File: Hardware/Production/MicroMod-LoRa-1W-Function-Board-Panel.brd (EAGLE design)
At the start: 96.6 x 150.8 mm, 202 parts, among them J1 MICROMOD_STANDARD, J11 MICROMOD_STANDARD, J2 MICROMOD_STANDARD, J3 MICROMOD_STANDARD, Q1 20V/4.2A/52mΩ/1.4W, Q10 600mA/40V, Q11 20V/4.2A/52mΩ/1.4W, Q12 600mA/40V, Q13 20V/4.2A/52mΩ/1.4W, Q14 600mA/40V, Q15 20V/4.2A/52mΩ/1.4W, Q16 600mA/40V, Q2 600mA/40V, Q3 20V/4.2A/52mΩ/1.4W, Q4 600mA/40V, Q5 20V/4.2A/52mΩ/1.4W, Q6 600mA/40V, Q7 20V/4.2A/52mΩ/1.4W, Q8 600mA/40V, Q9 20V/4.2A/52mΩ/1.4W, U1 EEPROM, U2 E19-915M30S, U3 EEPROM, U4 E19-915M30S, U5 E19-915M30S, U6 EEPROM, U7 E19-915M30S, U8 EEPROM

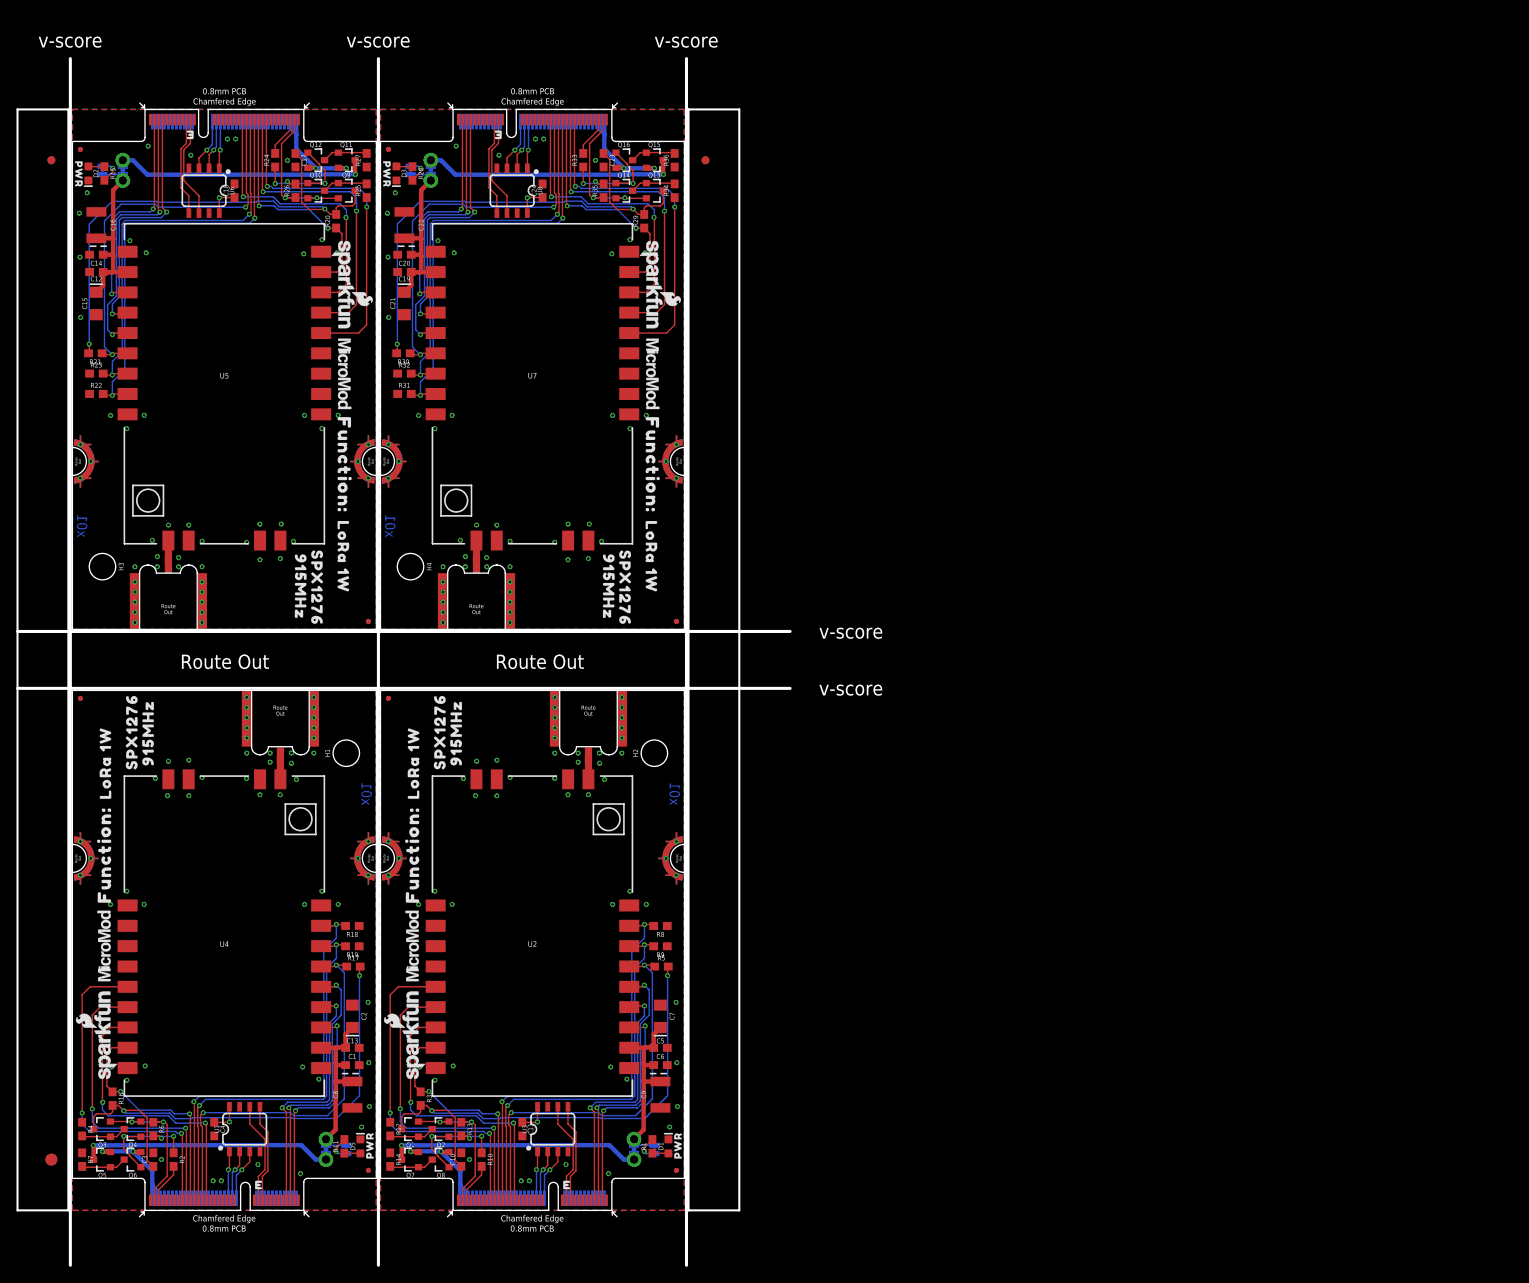
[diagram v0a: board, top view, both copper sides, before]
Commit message: Fix power control circuit. Add example sketch. Add x02 production panels.
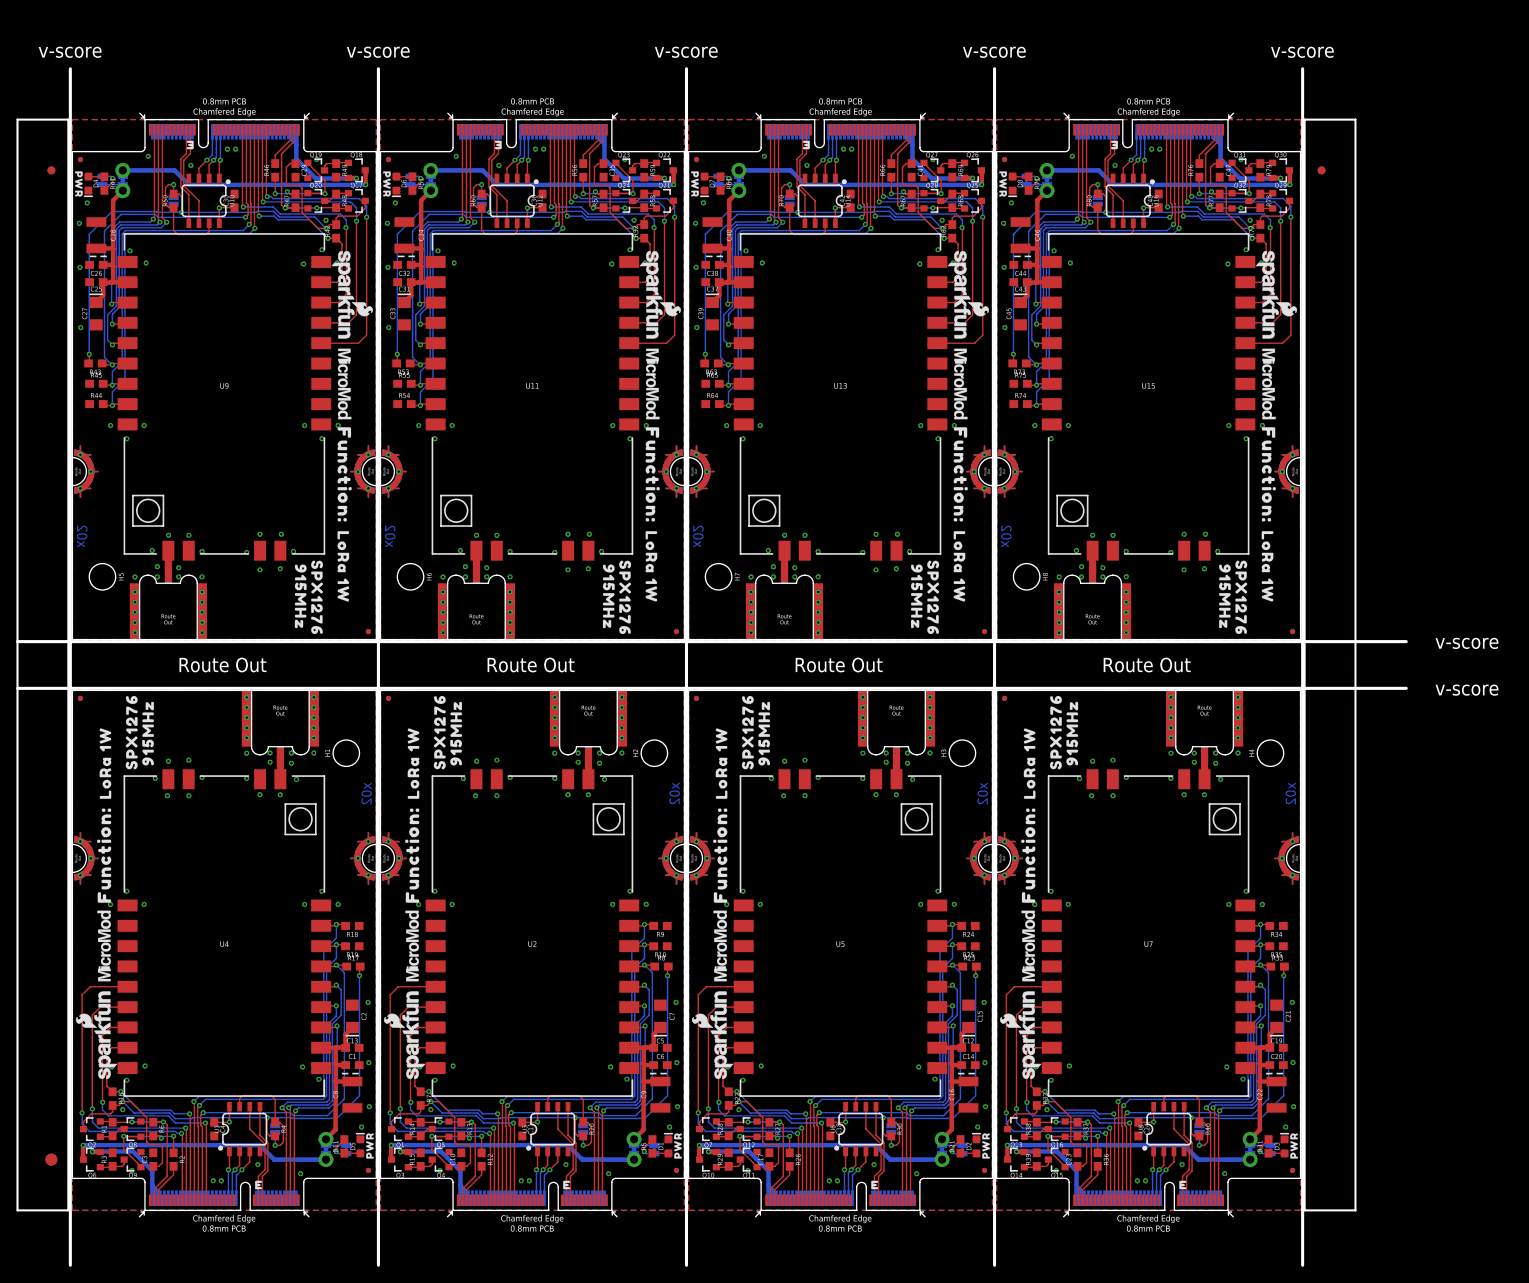
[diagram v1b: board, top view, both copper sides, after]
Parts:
- added C25, C31, C37, C43: 0.22uF, SparkFun-Capacitors:0603
- added C26, C29, C30, C32, C35, C36, C38, C41, C42, C44, C47, C48: 0.1uF, SparkFun-Capacitors:0603
- added C27, C33, C39, C45: 10uF, SparkFun-Capacitors:EIA3216
- added C28, C34, C40, C46: 47uF, SparkFun-Capacitors:EIA3528
- added D4, D6, D7, D8: RED, SparkFun-LED:LED-0603
- added E5, E6, E7, E8: RP-SMA, SparkFun-RF:SMA-EDGE-SMD
- added FD17, FD18, FD19, FD20, FD21, FD22, FD23, FD24, FD25, FD26, FD27, FD28, FD29, FD30, FD31, FD32: FIDUCIALUFIDUCIAL, SparkFun-Aesthetics:FIDUCIAL-MICRO
- added H5, H6, H7, H8: STAND-OFF, SparkFun-Hardware:STAND-OFF
- added J4, J5, J6, J7: MICROMOD_STANDARD, SparkFun-MicroMod-Function:M.2-CARD-E-22_FUNCTION_STANDARD
- added JP1, JP2, JP3, JP4, JP5, JP6, JP7, JP8: (no value), SparkFun-Jumpers:SMT-JUMPER_2_NO_SILK
- added LOGO13, LOGO15, LOGO16, LOGO18, LOGO19, LOGO21, LOGO22, LOGO24: SFE_LOGO_NAME_FLAME.1_INCH, SparkFun-Aesthetics:SFE_LOGO_NAME_FLAME_.1
- added LOGO14, LOGO17, LOGO20, LOGO23: OSHW-LOGOMINI, SparkFun-Aesthetics:OSHW-LOGO-MINI
- added MEAS4, MEAS5, MEAS6, MEAS7: (no value), SparkFun-Jumpers:COMBO-JUMPER_2_NC_TRACE
- added PWR_LED4, PWR_LED5, PWR_LED6, PWR_LED7: (no value), SparkFun-Jumpers:SMT-JUMPER_2_NC_TRACE_SILK
- added Q17, Q18, Q21, Q22, Q25, Q26, Q29, Q30: 20V/4.2A/52mΩ/1.4W, SparkFun-DiscreteSemi:SOT23-3
- added Q19, Q20, Q23, Q24, Q27, Q28, Q31, Q32: 5.8A/30V/35mΩ, SparkFun-DiscreteSemi:SOT23-3
- added R37, R42, R43, R44, R45, R47, R52, R53, R54, R55, R57, R62, R63, R64, R65, R67, R72, R73, R74, R75, R77: 100k, SparkFun-Resistors:0603
- added R38, R39, R40, R48, R49, R50, R58, R59, R60, R68, R69, R70, R78, R79, R80: 10k, SparkFun-Resistors:0603
- added R41, R51, R61, R71: 1k, SparkFun-Resistors:0603
- added R46, R56, R66, R76: 470, SparkFun-Resistors:0603
- added U$100, U$108, U$116, U$124, U$68, U$76, U$84, U$92: (no value), output:1W1
- added U$101, U$107, U$117, U$123, U$69, U$75, U$85, U$91: (no value), output:915MHZ2
- added U$102, U$105, U$118, U$121, U$70, U$73, U$86, U$89: (no value), output:LORA0
- added U$103, U$106, U$119, U$122, U$71, U$74, U$87, U$90: (no value), output:SPX12763
- added U$104, U$120, U$72, U$88: (no value), output:PWR0
- added U$109, U$111, U$125, U$127, U$60, U$62, U$77, U$79, U$93, U$95: (no value), output:FUNCTION#0
- added U$110, U$126, U$61, U$78, U$94: (no value), output:#PWR#0
- added U$112, U$128, U$64, U$80, U$96: (no value), output:#WP#0
- added U$113, U$114, U$65, U$66, U$81, U$82, U$97, U$98: (no value), SparkFun-MicroMod:MICROMOD_LOGO_.35
- added U$115, U$67, U$83, U$99: (no value), output:#MEAS#3
- added U10, U12, U14, U16: EEPROM, SparkFun-IC-Memory:SO08
- added U11, U13, U15, U9: E19-915M30S, SparkFun-RF:E19-915MS1W
- C16, C22, C8, C9: value 68uF -> 47uF
- Q10, Q14, Q2, Q6: value 600mA/40V -> 20V/4.2A/52mΩ/1.4W
- Q11, Q15, Q5, Q9: value 20V/4.2A/52mΩ/1.4W -> 5.8A/30V/35mΩ
- Q12, Q16, Q4, Q8: value 600mA/40V -> 5.8A/30V/35mΩ
- R1, R15, R28: value 1k -> 10k
- R10, R24, R33: value 470 -> 100k
- R12, R26, R36: value 100k -> 470
- R14, R20, R29, R3, R30, R4: value 100k -> 10k
- R21, R31, R5: value 100k -> 1k
- U$10, U$26: device SparkFun-MicroMod:MICROMOD_LOGO_.35 -> output:#WP#0
- U$12, U$31: device output:#MEAS#3 -> SparkFun-MicroMod:MICROMOD_LOGO_.35
- U$13: device output:1W1 -> output:#MEAS#3
- U$14: device output:915MHZ2 -> output:1W1
- U$15: device output:LORA0 -> output:915MHZ2
- U$16, U$19: device output:SPX12763 -> output:LORA0
- U$17: device output:PWR0 -> output:SPX12763
- U$18: device output:LORA0 -> output:PWR0
- U$20: device output:915MHZ2 -> output:SPX12763
- U$21: device output:1W1 -> output:915MHZ2
- U$22, U$59: device output:FUNCTION#0 -> output:1W1
- U$23: device output:#PWR#0 -> output:FUNCTION#0
- U$24: device output:FUNCTION#0 -> output:#PWR#0
- U$25, U$46: device SparkFun-MicroMod:MICROMOD_LOGO_.35 -> output:FUNCTION#0
- U$32, U$48: device output:1W1 -> SparkFun-MicroMod:MICROMOD_LOGO_.35
- U$33: device output:915MHZ2 -> output:#MEAS#3
- U$34: device output:LORA0 -> output:1W1
- U$35: device output:SPX12763 -> output:915MHZ2
- U$36: device output:PWR0 -> output:LORA0
- U$38: device output:LORA0 -> output:SPX12763
- U$39: device output:SPX12763 -> output:PWR0
- U$40: device output:915MHZ2 -> output:LORA0
- U$41: device output:1W1 -> output:SPX12763
- U$42: device output:FUNCTION#0 -> output:915MHZ2
- U$43: device output:#PWR#0 -> output:1W1
- U$45: device SparkFun-MicroMod:MICROMOD_LOGO_.35 -> output:#PWR#0
- U$47: device output:#MEAS#3 -> output:#WP#0
- U$49: device output:915MHZ2 -> SparkFun-MicroMod:MICROMOD_LOGO_.35
- U$50: device output:LORA0 -> output:#MEAS#3
- U$51: device output:SPX12763 -> output:1W1
- U$52: device output:PWR0 -> output:915MHZ2
- U$55: device output:915MHZ2 -> output:PWR0
- U$56: device output:1W1 -> output:LORA0
- U$57: device output:FUNCTION#0 -> output:SPX12763
- U$58: device output:#PWR#0 -> output:915MHZ2
- moved FD13 170.5 mm to (152.5, 5.00), turned to 90 degrees
- moved FD15 170.5 mm to (152.5, 5.00), turned to 270 degrees
- moved FD11 170.5 mm to (114.0, 5.00), turned to 270 degrees
- moved FD9 170.5 mm to (114.0, 5.00), turned to 90 degrees
- moved D3 164.7 mm to (151.5, 8.00), turned to 90 degrees
- moved D2 164.7 mm to (113.0, 8.00), turned to 90 degrees
- moved PWR_LED3 162.9 mm to (149.8, 7.62), turned to 90 degrees
- moved PWR_LED2 162.9 mm to (111.3, 7.62), turned to 90 degrees
- moved MEAS3 159.6 mm to (147.2, 7.62), turned to 90 degrees
- moved MEAS2 159.6 mm to (108.7, 7.62), turned to 90 degrees
- moved J3 157.7 mm to (134.5, 0.00), turned to 0 degrees
- moved J2 157.7 mm to (96.0, 0.00), turned to 0 degrees
- moved C22 153.9 mm to (150.5, 14.5), turned to 90 degrees
- moved C16 153.9 mm to (112.0, 14.5), turned to 90 degrees
- moved C20 148.8 mm to (150.5, 18.2), turned to 0 degrees
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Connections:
- removed net N$10 (its old number): Q1.1, Q2.3, R12.2
- removed net N$17 (its old number): Q10.3, Q9.1, R25.2
- removed net N$24 (its old number): Q15.1, Q16.3, R36.2
- new net 3.3V4: C29.1, C30.1, Q17.3, R42.2, R43.2, R50.2, U10.8
- new net 3.3V5: C35.1, C36.1, Q21.3, R52.2, R53.2, R60.2, U12.8
- new net 3.3V6: C41.1, C42.1, Q25.3, R62.2, R63.2, R70.2, U14.8
- new net 3.3V7: C47.1, C48.1, Q29.3, R72.2, R73.2, R80.2, U16.8
- new net 3.3V_IN4: J4.73, Q17.2, R47.1, R48.2
- new net 3.3V_IN5: J5.73, Q21.2, R57.1, R58.2
- new net 3.3V_IN6: J6.73, Q25.2, R67.1, R68.2
- new net 3.3V_IN7: J7.73, Q29.2, R77.1, R78.2
- new net 5V4: C25.1, C26.1, C27.+, C28.A, MEAS4.2, MEAS4.4, PWR_LED4.2, U9.11
- new net 5V5: C31.1, C32.1, C33.+, C34.A, MEAS5.2, MEAS5.4, PWR_LED5.2, U11.11
- new net 5V6: C37.1, C38.1, C39.+, C40.A, MEAS6.2, MEAS6.4, PWR_LED6.2, U13.11
- new net 5V7: C43.1, C44.1, C45.+, C46.A, MEAS7.2, MEAS7.4, PWR_LED7.2, U15.11
- new net A12: J4.36, U10.1
- new net A13: J4.32, U10.3
- new net A14: J4.34, U10.2
- new net A15: J5.36, U12.1
- new net A16: J5.32, U12.3
- new net A17: J5.34, U12.2
- new net A18: J6.36, U14.1
- new net A19: J6.32, U14.3
- new net A20: J6.34, U14.2
- new net A21: J7.36, U16.1
- new net A22: J7.32, U16.3
- new net A23: J7.34, U16.2
- new net GND4: C25.2, C26.2, C27.-, C28.C, C29.2, C30.2, D4.C, E5.GND@0, E5.GND@1, J4.1, J4.33, J4.39, J4.45, J4.75, J4.GND1, J4.GND2, J4.GND3, J4.GND4, J4.GND5, J4.GND6, JP5.1, Q19.2, Q20.2, R44.1, R45.1, U10.4, U9.1, U9.10, U9.18, U9.20, U9.21, U9.22, U9.9
- new net GND5: C31.2, C32.2, C33.-, C34.C, C35.2, C36.2, D6.C, E6.GND@0, E6.GND@1, J5.1, J5.33, J5.39, J5.45, J5.75, J5.GND1, J5.GND2, J5.GND3, J5.GND4, J5.GND5, J5.GND6, JP6.1, Q23.2, Q24.2, R54.1, R55.1, U11.1, U11.10, U11.18, U11.20, U11.21, U11.22, U11.9, U12.4
- new net GND6: C37.2, C38.2, C39.-, C40.C, C41.2, C42.2, D7.C, E7.GND@0, E7.GND@1, J6.1, J6.33, J6.39, J6.45, J6.75, J6.GND1, J6.GND2, J6.GND3, J6.GND4, J6.GND5, J6.GND6, JP7.1, Q27.2, Q28.2, R64.1, R65.1, U13.1, U13.10, U13.18, U13.20, U13.21, U13.22, U13.9, U14.4
- new net GND7: C43.2, C44.2, C45.-, C46.C, C47.2, C48.2, D8.C, E8.GND@0, E8.GND@1, J7.1, J7.33, J7.39, J7.45, J7.75, J7.GND1, J7.GND2, J7.GND3, J7.GND4, J7.GND5, J7.GND6, JP8.1, Q31.2, Q32.2, R74.1, R75.1, U15.1, U15.10, U15.18, U15.20, U15.21, U15.22, U15.9, U16.4
- new net I2C_SCL4: J4.21, U10.6
- new net I2C_SCL5: J5.21, U12.6
- new net I2C_SCL6: J6.21, U14.6
- new net I2C_SCL7: J7.21, U16.6
- new net I2C_SDA4: J4.19, U10.5
- new net I2C_SDA5: J5.19, U12.5
- new net I2C_SDA6: J6.19, U14.5
- new net I2C_SDA7: J7.19, U16.5
- new net LORA_!CS!4: J4.49, R43.1, U9.15
- new net LORA_!CS!5: J5.49, R53.1, U11.15
- new net LORA_!CS!6: J6.49, R63.1, U13.15
- new net LORA_!CS!7: J7.49, R73.1, U15.15
- new net LORA_!RST!4: J4.55, R42.1, U9.8
- new net LORA_!RST!5: J5.55, R52.1, U11.8
- new net LORA_!RST!6: J6.55, R62.1, U13.8
- new net LORA_!RST!7: J7.55, R72.1, U15.8
- new net LORA_D12: J4.47, U9.7
- new net LORA_D13: J4.57, U9.6
- new net LORA_D14: J4.59, U9.5
- new net LORA_D15: J5.47, U11.7
- new net LORA_D16: J5.57, U11.6
- new net LORA_D17: J5.59, U11.5
- new net LORA_D18: J6.47, U13.7
- new net LORA_D19: J6.57, U13.6
- new net LORA_D20: J6.59, U13.5
- new net LORA_D21: J7.47, U15.7
- new net LORA_D22: J7.57, U15.6
- new net LORA_D23: J7.59, U15.5
- new net LORA_RXEN4: J4.53, R44.2, U9.17
- new net LORA_RXEN5: J5.53, R54.2, U11.17
- new net LORA_RXEN6: J6.53, R64.2, U13.17
- new net LORA_RXEN7: J7.53, R74.2, U15.17
- new net LORA_TXEN4: J4.51, R45.2, U9.16
- new net LORA_TXEN5: J5.51, R55.2, U11.16
- new net LORA_TXEN6: J6.51, R65.2, U13.16
- new net LORA_TXEN7: J7.51, R75.2, U15.16
- new net N$15: PWR_LED2.1, R21.2
- new net N$21: JP3.2, R30.1, U6.7
- new net N$25: J3.71, R36.2
- new net N$26: Q13.1, Q16.3, R38.1
- new net N$27: Q14.1, Q15.3, R39.1
- new net N$28: JP4.2, R40.1, U8.7
- new net N$29: PWR_LED4.1, R41.2
- new net N$30: D4.A, R41.1
- new net N$31: E5.SIG, U9.19
- new net N$32: J4.71, R46.2
- new net N$33: Q17.1, Q20.3, R48.1
- new net N$34: Q18.1, Q19.3, R49.1
- new net N$35: JP5.2, R50.1, U10.7
- new net N$36: PWR_LED5.1, R51.2
- new net N$37: D6.A, R51.1
- new net N$38: E6.SIG, U11.19
- new net N$39: J5.71, R56.2
- new net N$40: Q21.1, Q24.3, R58.1
- new net N$41: Q22.1, Q23.3, R59.1
- new net N$42: JP6.2, R60.1, U12.7
- new net N$43: PWR_LED6.1, R61.2
- new net N$44: D7.A, R61.1
- new net N$45: E7.SIG, U13.19
- new net N$46: J6.71, R66.2
- new net N$47: Q25.1, Q28.3, R68.1
- new net N$48: Q26.1, Q27.3, R69.1
- new net N$49: JP7.2, R70.1, U14.7
- new net N$50: PWR_LED7.1, R71.2
- new net N$51: D8.A, R71.1
- new net N$52: E8.SIG, U15.19
- new net N$53: J7.71, R76.2
- new net N$54: Q29.1, Q32.3, R78.1
- new net N$55: Q30.1, Q31.3, R79.1
- new net N$56: JP8.2, R80.1, U16.7
- new net N$7: JP1.2, R4.1, U1.7
- new net PWR_EN4: Q19.1, Q20.1, R46.1, R47.2
- new net PWR_EN5: Q23.1, Q24.1, R56.1, R57.2
- new net PWR_EN6: Q27.1, Q28.1, R66.1, R67.2
- new net PWR_EN7: Q31.1, Q32.1, R76.1, R77.2
- new net SPI_CIPO4: J4.7, U9.13
- new net SPI_CIPO5: J5.7, U11.13
- new net SPI_CIPO6: J6.7, U13.13
- new net SPI_CIPO7: J7.7, U15.13
- new net SPI_COPI4: J4.5, U9.14
- new net SPI_COPI5: J5.5, U11.14
- new net SPI_COPI6: J6.5, U13.14
- new net SPI_COPI7: J7.5, U15.14
- new net SPI_SCK4: J4.3, U9.12
- new net SPI_SCK5: J5.3, U11.12
- new net SPI_SCK6: J6.3, U13.12
- new net SPI_SCK7: J7.3, U15.12
- new net VCC4: MEAS4.1, MEAS4.3, Q18.3
- new net VCC5: MEAS5.1, MEAS5.3, Q22.3
- new net VCC6: MEAS6.1, MEAS6.3, Q26.3
- new net VCC7: MEAS7.1, MEAS7.3, Q30.3
- new net VCC_IN4: J4.72, J4.74, Q18.2, R49.2
- new net VCC_IN5: J5.72, J5.74, Q22.2, R59.2
- new net VCC_IN6: J6.72, J6.74, Q26.2, R69.2
- new net VCC_IN7: J7.72, J7.74, Q30.2, R79.2
- net 3.3V: now also Q2.3, R4.2; no longer Q3.3
- net 3.3V1: now also R20.2, R7.2, R8.2; no longer R3.2, R5.2
- net 3.3V2: now also Q7.3, R22.2, R23.2, R30.2; no longer Q9.3, R20.2, R21.2
- net 3.3V3: now also R32.2, R33.2, R40.2; no longer R29.2, R30.2
- net 3.3V_IN: now also Q2.2, R1.2; no longer Q3.2, Q4.2
- net 3.3V_IN1: now also R14.2; no longer Q2.2
- net 3.3V_IN2: now also Q7.2, R27.1, R28.2; no longer Q10.2, Q9.2, R26.1
- net 3.3V_IN3: now also R37.1, R38.2; no longer Q14.2, R35.1
- net GND: now also JP1.1, Q8.2, Q9.2; no longer R4.1, R7.1, U1.7
- net GND1: now also JP2.1, Q4.2, Q5.2, R10.1; no longer R12.1, R14.1, R8.1, U3.7
- net GND2: now also JP3.1, Q11.2, Q12.2, R24.1; no longer R22.1, R23.1, R27.1, U6.7
- net GND3: now also JP4.1, Q15.2, Q16.2, R35.1; no longer R31.1, R32.1, R36.1, U8.7
- net LORA_!CS!1: now also R8.1; no longer R5.1
- net LORA_!CS!2: now also R23.1; no longer R21.1
- net LORA_!CS!3: now also R33.1; no longer R30.1
- net LORA_!RST!1: now also R7.1; no longer R3.1
- net LORA_!RST!2: now also R22.1; no longer R20.1
- net LORA_!RST!3: now also R32.1; no longer R29.1
- net LORA_RXEN1: now also R9.2; no longer R8.2
- net LORA_RXEN2: now also R24.2; no longer R22.2
- net LORA_RXEN3: now also R34.2; no longer R31.2
- net LORA_TXEN1: now also R10.2; no longer R9.2
- net LORA_TXEN2: now also R25.2; no longer R23.2
- net LORA_TXEN3: now also R35.2; no longer R32.2
- net N$11: now also J1.71, R12.2; no longer Q5.1, Q6.3, R7.2
- net N$12: now also Q1.1, Q5.3, R14.1; no longer Q7.1, Q8.3, R14.2
- net N$13: now also Q3.1, Q4.3, R15.1; no longer PWR_LED2.1, R15.2
- net N$14: now also JP2.2, R20.1, U3.7; no longer D2.A, R15.1
- net N$16: now also D2.A, R21.1; no longer J2.71, R24.2
- net N$18: now also J2.71, R26.2; no longer Q11.1, Q12.3, R27.2
- net N$19: now also Q12.3, Q7.1, R28.1; no longer PWR_LED3.1, R28.2
- net N$2: now also Q2.1, Q8.3, R1.1; no longer PWR_LED1.1, R1.2
- net N$20: now also Q10.1, Q11.3, R29.1; no longer D3.A, R28.1
- net N$22: now also PWR_LED3.1, R31.2; no longer J3.71, R33.2
- net N$23: now also D3.A, R31.1; no longer Q13.1, Q14.3, R34.2
- net N$3: now also Q6.1, Q9.3, R3.1; no longer D1.A, R1.1
- net N$8: now also PWR_LED1.1, R5.2; no longer J1.71, R10.2
- net N$9: now also D1.A, R5.1; no longer Q3.1, Q4.3, R4.2
- net PWR_EN: now also Q8.1, Q9.1; no longer Q4.1, Q6.1
- net PWR_EN1: now also Q4.1, Q5.1, R12.1; no longer Q2.1, Q8.1, R10.1
- net PWR_EN2: now also Q11.1, R26.1, R27.2; no longer Q10.1, R24.1, R26.2
- net PWR_EN3: now also Q15.1, R36.1, R37.2; no longer Q14.1, R33.1, R35.2
- net VCC: now also Q6.3; no longer Q5.3
- net VCC1: now also Q3.3; no longer Q7.3
- net VCC2: now also Q10.3; no longer Q11.3
- net VCC3: now also Q14.3; no longer Q15.3
- net VCC_IN: now also R3.2; no longer Q5.2
- net VCC_IN1: now also Q3.2, R15.2; no longer Q7.2, Q8.2
- net VCC_IN2: now also Q10.2, R29.2; no longer Q11.2, Q12.2
- net VCC_IN3: now also Q14.2, R39.2; no longer Q15.2, Q16.2
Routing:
- net 3.3V7: track 0.00 -> 75.2 mm, vias 0 -> 4
- net 3.3V6: track 0.00 -> 75.2 mm, vias 0 -> 4
- net 3.3V5: track 0.00 -> 75.2 mm, vias 0 -> 4
- net 3.3V4: track 0.00 -> 75.2 mm, vias 0 -> 4
- net LORA_RXEN4: track 0.00 -> 54.1 mm, vias 0 -> 2
- net LORA_RXEN6: track 0.00 -> 54.1 mm, vias 0 -> 2
- net LORA_RXEN5: track 0.00 -> 54.1 mm, vias 0 -> 2
- net LORA_RXEN7: track 0.00 -> 54.1 mm, vias 0 -> 2
- net LORA_TXEN4: track 0.00 -> 50.9 mm, vias 0 -> 2
- net LORA_TXEN5: track 0.00 -> 50.9 mm, vias 0 -> 2
- net LORA_TXEN7: track 0.00 -> 50.9 mm, vias 0 -> 2
- net LORA_TXEN6: track 0.00 -> 50.9 mm, vias 0 -> 2
- net LORA_!CS!7: track 0.00 -> 50.3 mm, vias 0 -> 2
- net LORA_!CS!6: track 0.00 -> 50.3 mm, vias 0 -> 2
- net LORA_!CS!5: track 0.00 -> 50.3 mm, vias 0 -> 2
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- added copper zone on layer 1, net GND4
- added copper zone on layer 16, net GND4
- added copper zone on layer 1, net GND5
- added copper zone on layer 16, net GND5
- added copper zone on layer 1, net GND6
- added copper zone on layer 16, net GND6
- added copper zone on layer 1, net GND7
- added copper zone on layer 16, net GND7
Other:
- board size 96.6 x 150.8 mm -> 173.6 x 149.6 mm
- board text added: "x02"
- board text removed: "x01"

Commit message: Update version to v10.
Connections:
- removed net N$14 (its old number): JP2.2, R20.1, U3.7
- removed net N$21 (its old number): JP3.2, R30.1, U6.7
- removed net N$28 (its old number): JP4.2, R40.1, U8.7
- removed net N$35 (its old number): JP5.2, R50.1, U10.7
- removed net N$42 (its old number): JP6.2, R60.1, U12.7
- removed net N$49: JP7.2, R70.1, U14.7
- removed net N$56: JP8.2, R80.1, U16.7
- removed net N$7 (its old number): JP1.2, R4.1, U1.7
- new net EWP: J11.40, JP1.2, R4.1, U1.7
- new net EWP1: J1.40, JP2.2, R20.1, U3.7
- new net EWP2: J2.40, JP3.2, R30.1, U6.7
- new net EWP3: J3.40, JP4.2, R40.1, U8.7
- new net EWP4: J4.40, JP5.2, R50.1, U10.7
- new net EWP5: J5.40, JP6.2, R60.1, U12.7
- new net EWP6: J6.40, JP7.2, R70.1, U14.7
- new net EWP7: J7.40, JP8.2, R80.1, U16.7
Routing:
- net EWP5: track 0.00 -> 28.9 mm, vias 0 -> 3
- net EWP4: track 0.00 -> 28.9 mm, vias 0 -> 3
- net EWP6: track 0.00 -> 28.9 mm, vias 0 -> 3
- net EWP2: track 0.00 -> 28.9 mm, vias 0 -> 3
- net EWP7: track 0.00 -> 28.9 mm, vias 0 -> 3
- net EWP: track 0.00 -> 28.9 mm, vias 0 -> 3
- net EWP3: track 0.00 -> 28.9 mm, vias 0 -> 3
- net EWP1: track 0.00 -> 28.9 mm, vias 0 -> 3
- net N$7 (its old number): track 14.7 -> 0.00 mm, vias 1 -> 0
- net N$14 (its old number): track 14.7 -> 0.00 mm, vias 1 -> 0
- net N$42 (its old number): track 14.7 -> 0.00 mm, vias 1 -> 0
- net N$35 (its old number): track 14.7 -> 0.00 mm, vias 1 -> 0
- net N$21 (its old number): track 14.7 -> 0.00 mm, vias 1 -> 0
- net N$49: track 14.7 -> 0.00 mm, vias 1 -> 0
- net N$28 (its old number): track 14.7 -> 0.00 mm, vias 1 -> 0
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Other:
- board size 173.6 x 149.6 mm -> 167.2 x 149.6 mm
- board text added: "v10"
- board text removed: "x02"
